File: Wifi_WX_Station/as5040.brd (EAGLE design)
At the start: 25.4 x 20 mm, 8 parts, among them U1 SI7021-DFN6

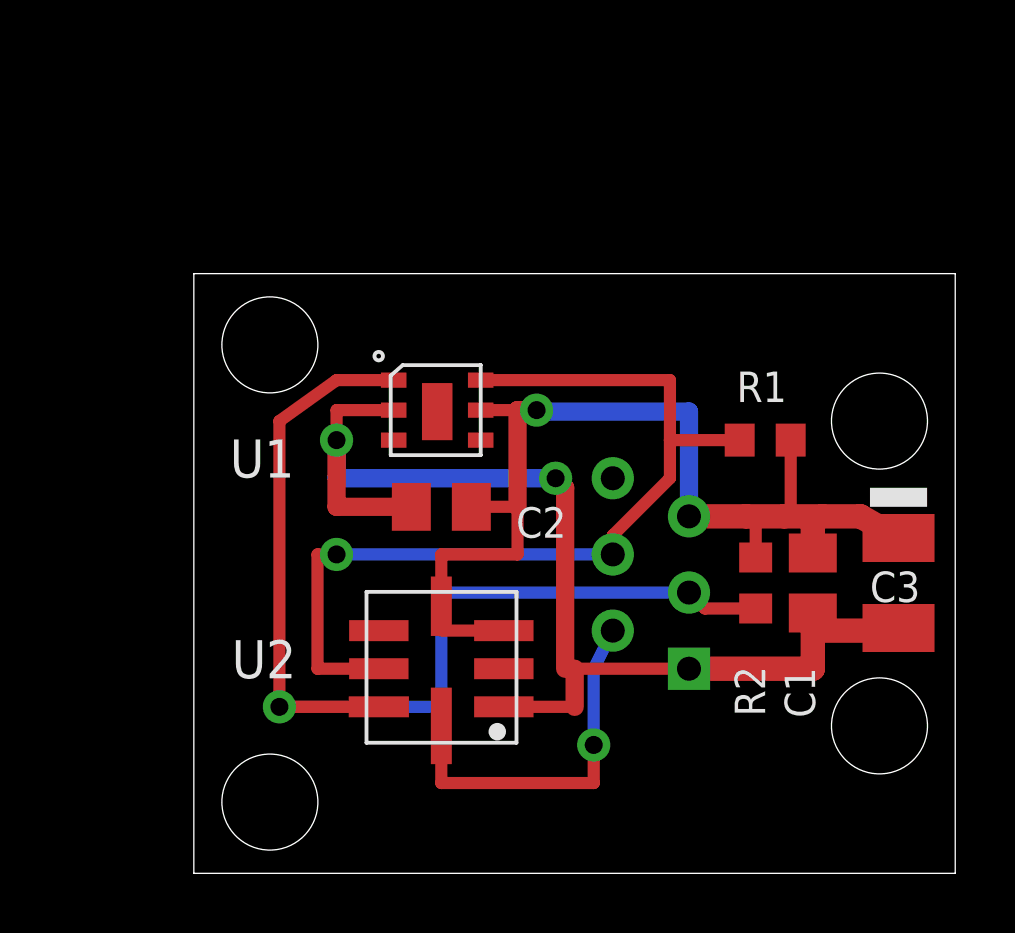
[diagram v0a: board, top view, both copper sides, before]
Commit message: Added multiple new boards - H-pwrdist- Insp_Wind_enc, 5040 etc..
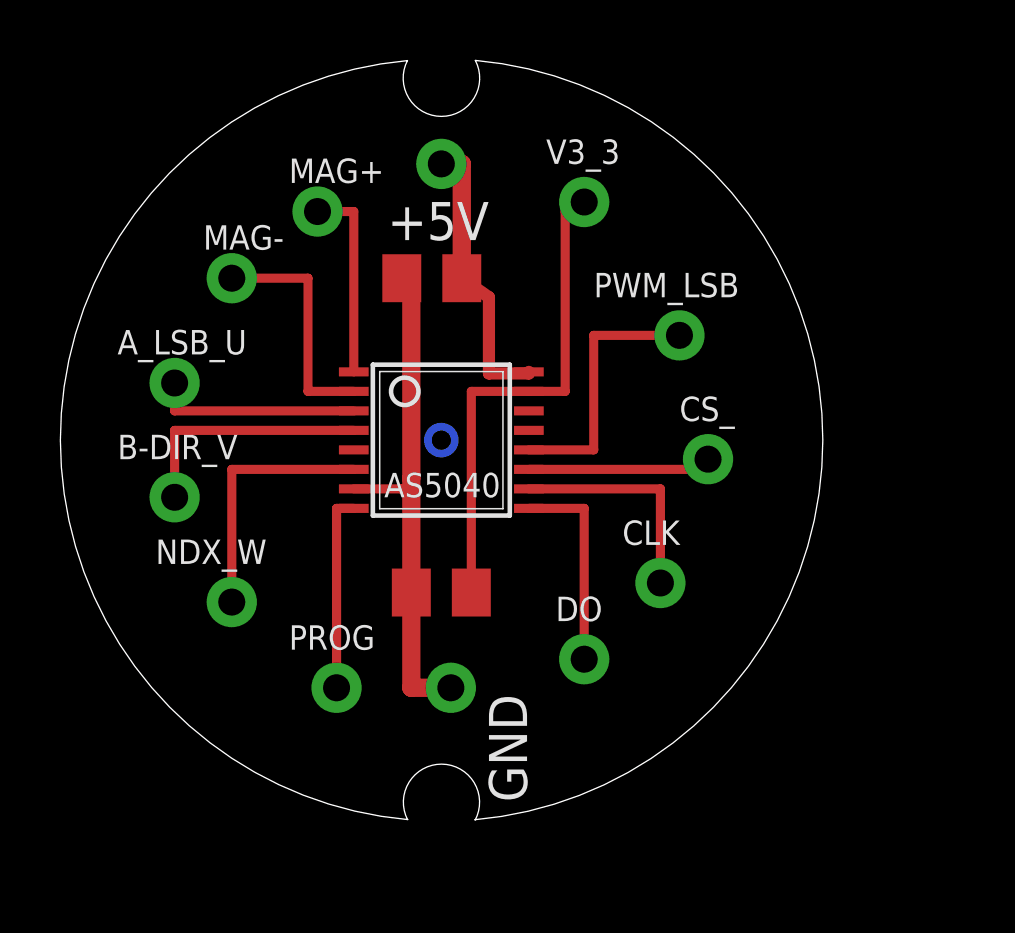
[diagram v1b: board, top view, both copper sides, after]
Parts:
- removed C2: 100nF, rcl:C0805K
- removed C3: 22uF/10V, rcl:SMC_B
- removed JP2: RJ11-6HOR_LP, wifi_WX:RJ11_HOR_LP
- removed R1, R2: 470o, rcl:R0603
- removed U1: SI7021-DFN6, wifi_WX:DFN-6_SILABS
- removed U2: (no value), 1AA_Stofer:LCC8
- added +5V, A_LSB_U, B-DIR_V, CLK, CS_, DO, GND, MAG+, MAG-, NDX_W, PROG, PWM_LSB, V3_3: TPSOL, wifi_WX:TP_SOL
- added C5: 1uF, rcl:C0805K
- added U$2: AS5040, 1AA_Stofer:TSSOP16
- C1: value 100nF -> 1uF
- moved C1 12.4 mm to (14.0, 8.89), turned to 180 degrees
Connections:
- removed net +3V3: C1.1, C2.1, C3.+, JP2.P$5, R1.2, R2.2, U1.P$5, U2.P$3, U2.P$4
- removed net GND: C1.2, C2.2, C3.-, JP2.P$1, U1.P$2, U2.P$1
- removed net SCL: JP2.P$4, R1.1, U1.P$6, U2.P$6
- removed net SDA: JP2.P$3, R2.1, U1.P$1, U2.P$7
- removed net XCLR: JP2.P$2, U2.P$8
- new net N$10: PROG.P$1, U$2.8
- new net N$11: PWM_LSB.P$1, U$2.12
- new net N$12: CS_.P$1, U$2.11
- new net N$13: CLK.P$1, U$2.10
- new net N$14: DO.P$1, U$2.9
- new net N$2: C1.2, C5.2, GND.P$1, U$2.7
- new net N$3: +5V.P$1, C5.1, U$2.16
- new net N$4: C1.1, U$2.15, V3_3.P$1
- new net N$5: MAG+.P$1, U$2.1
- new net N$6: MAG-.P$1, U$2.2
- new net N$7: A_LSB_U.P$1, U$2.3
- new net N$8: B-DIR_V.P$1, U$2.4
- new net N$9: NDX_W.P$1, U$2.6
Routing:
- net GND: track 39.3 -> 0.00 mm, vias 2 -> 0
- net +3V3: track 37.3 -> 0.00 mm, vias 1 -> 0
- net SDA: track 37.0 -> 0.00 mm, vias 1 -> 0
- net SCL: track 30.9 -> 0.00 mm, vias 1 -> 0
- net N$2: track 0.00 -> 17.1 mm
- net N$4: track 0.00 -> 16.8 mm
- net XCLR: track 12.2 -> 0.00 mm, vias 1 -> 0
- net N$3: track 0.00 -> 9.52 mm
- net N$11: track 0.00 -> 8.84 mm
- net N$9: track 0.00 -> 8.49 mm
- net N$8: track 0.00 -> 8.20 mm
- net N$6: track 0.00 -> 7.84 mm
- net N$13: track 0.00 -> 7.52 mm
- net N$10: track 0.00 -> 7.19 mm
- net N$7: track 0.00 -> 6.90 mm
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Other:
- board size 25.4 x 20 mm -> 25.4 x 25.3 mm
- board text added: "+5V"
- board text added: "AS5040"
- board text removed: "Baro-Temp-Hyg"
- board text removed: "Rev B.2"
- board text removed: "U2"
- board text removed: "Wunder Weather 2014"
